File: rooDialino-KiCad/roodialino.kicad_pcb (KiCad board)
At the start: 2 copper layers, 65 x 30 mm, 54 parts, among them J1 Raspi Connector, J2 ICSP, J3 FTDI, J4 2nd IRX, J5 IR LED, Q1 2N7002, Q2 2N7002, Q3 2N7002, SW1 SW_Push, U1 ATmega328P, U2 TSOP34838, U3 TXS0108EPW, Y1 16 MHz

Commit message: Some final (?) bling
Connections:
- J5 pad 1: Net-(J5-Pad1) -> Net-(D8-Pad1)
- J5 pad 2: Net-(D8-Pad1) -> Net-(J5-Pad2)
- R11 pad 2: Net-(J5-Pad1) -> Net-(J5-Pad2)
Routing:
- net Net-(J5-Pad2): track 0.00 -> 6.35 mm
- net Net-(J5-Pad1): track 3.19 -> 0.00 mm
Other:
- board text removed: "A"

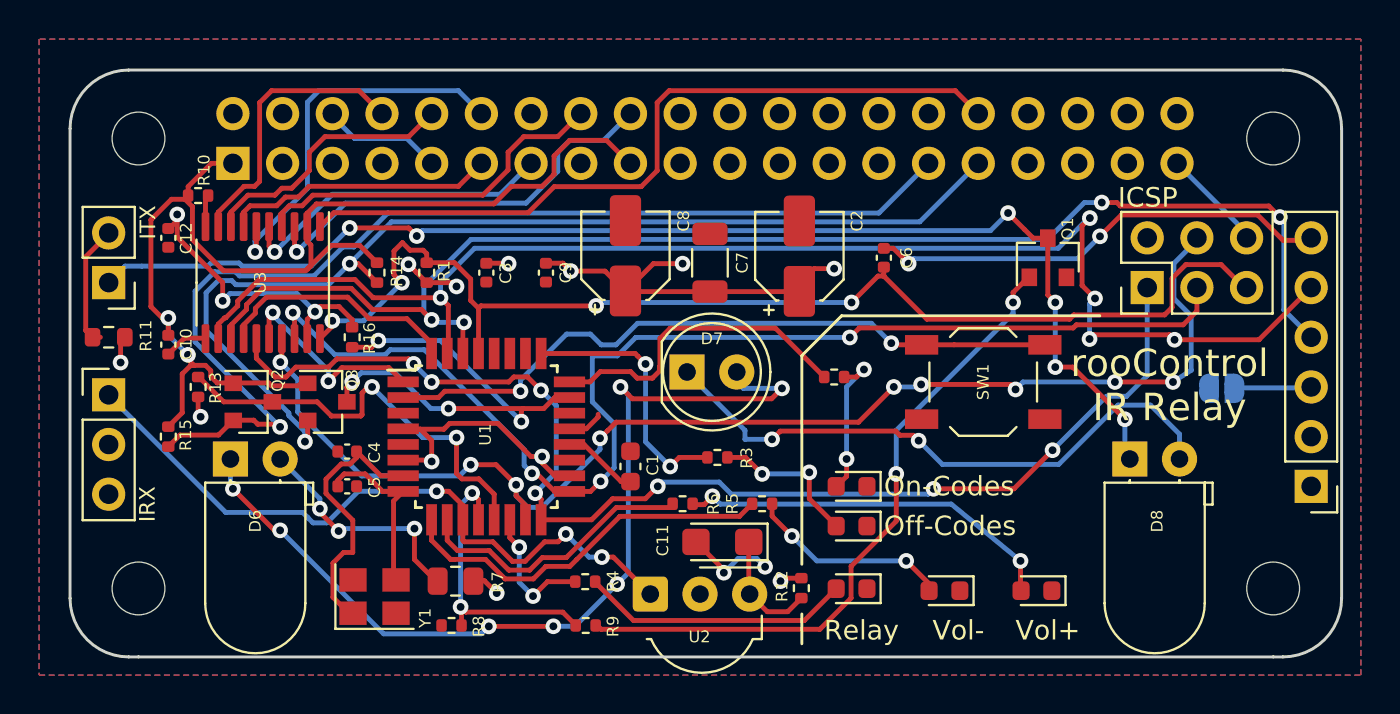
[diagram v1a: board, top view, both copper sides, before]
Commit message: Add Tooling Holes
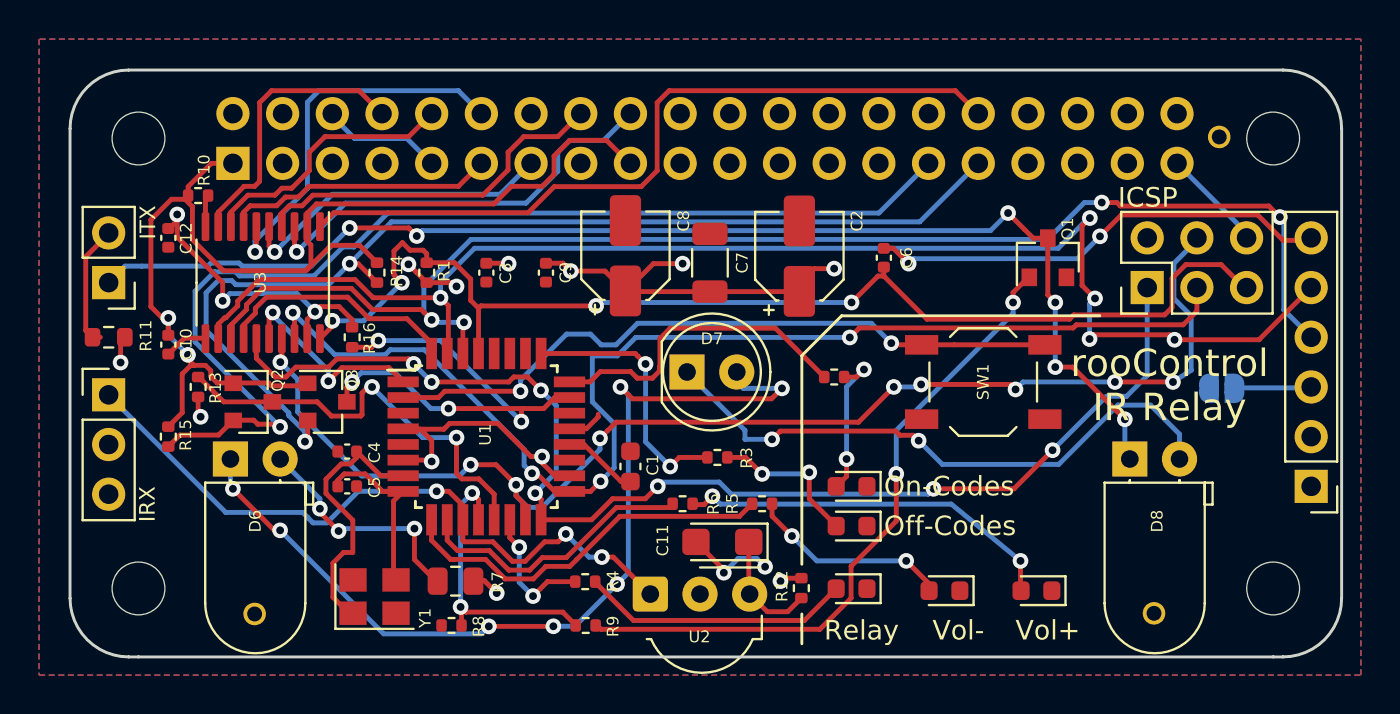
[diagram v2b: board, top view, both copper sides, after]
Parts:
- added REF**: JLCPCB Tooling Hole, MountingHole:JLCPCB Tooling Hole, F.Cu at (174.3, 92.5)
- added REF**: JLCPCB Tooling Hole, MountingHole:JLCPCB Tooling Hole, F.Cu at (170.9, 116.8)
- added REF**: JLCPCB Tooling Hole, MountingHole:JLCPCB Tooling Hole, F.Cu at (125.0, 116.9)
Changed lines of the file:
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@@
     (tracks 819)
     (zones 0)
-    (modules 54)
+    (modules 57)
     (nets 73)
   )
@@
     (add_net "Net-(U1-Pad28)")
   )
+  (module "MountingHole:JLCPCB Tooling Hole" (layer F.Cu)
+    (at 174.276 92.488)
+    (fp_text reference REF** (at 0.0254 2.0828) (layer F.SilkS) hide
+      (effects (font (size 1 1) (thickness 0.15)))
+    )
+    (fp_text value "JLCPCB Tooling Hole" (at -0.3556 -1.7272) (layer F.Fab)
+      (effects (font (size 1 1) (thickness 0.15)))
+    )
+    (pad "" np_thru_hole circle (at 2 2) (size 1.152 1.152) (drill 0.762) (layers *.Cu *.Mask)
+      (solder_mask_margin 0.148))
+  )
+  (module "MountingHole:JLCPCB Tooling Hole" (layer F.Cu)
+    (at 170.942 116.84)
+    (fp_text reference REF** (at 0.0254 2.0828) (layer F.SilkS) hide
+      (effects (font (size 1 1) (thickness 0.15)))
+    )
+    (fp_text value "JLCPCB Tooling Hole" (at -0.3556 -1.7272) (layer F.Fab)
+      (effects (font (size 1 1) (thickness 0.15)))
+    )
+    (pad "" np_thru_hole circle (at 2 2) (size 1.152 1.152) (drill 0.762) (layers *.Cu *.Mask)
+      (solder_mask_margin 0.148))
+  )
+  (module "MountingHole:JLCPCB Tooling Hole" (layer F.Cu)
+    (at 124.968 116.872)
+    (fp_text reference REF** (at 0.0254 2.0828) (layer F.SilkS) hide
+      (effects (font (size 1 1) (thickness 0.15)))
+    )
+    (fp_text value "JLCPCB Tooling Hole" (at -0.3556 -1.7272) (layer F.Fab)
+      (effects (font (size 1 1) (thickness 0.15)))
+    )
+    (pad "" np_thru_hole circle (at 2 2) (size 1.152 1.152) (drill 0.762) (layers *.Cu *.Mask)
+      (solder_mask_margin 0.148))
+  )
   (module Capacitor_Tantalum_SMD:CP_EIA-3216-18_Kemet-A (layer F.Cu)
     (at 150.876 115.189 180)
@@
       (effects (font (size 0.8 0.8) (thickness 0.12)))
     )
-    (pad 1 smd roundrect (at -1.35 0 180) (size 1.4 1.35) (layers F.Cu F.Paste F.Mask) (roundrect_rratio 0.185185)
+    (pad 1 smd roundrect (at -1.35 0 180) (size 1.4 1.35) (layers F.Cu F.Paste F.Mask) (roundrect_rratio 0.1851844444444445)
       (net 69 "Net-(C11-Pad1)"))
-    (pad 2 smd roundrect (at 1.35 0 180) (size 1.4 1.35) (layers F.Cu F.Paste F.Mask) (roundrect_rratio 0.185185)
+    (pad 2 smd roundrect (at 1.35 0 180) (size 1.4 1.35) (layers F.Cu F.Paste F.Mask) (roundrect_rratio 0.1851844444444445)
       (net 6 GNDD))
     (model ${KISYS3DMOD}/Capacitor_Tantalum_SMD.3dshapes/CP_EIA-3216-18_Kemet-A.wrl
@@
       (effects (font (size 0.5 0.5) (thickness 0.08)))
     )
-    (pad 1 smd roundrect (at -0.9125 0 180) (size 1.025 1.4) (layers F.Cu F.Paste F.Mask) (roundrect_rratio 0.2439014634146341)
+    (pad 1 smd roundrect (at -0.9125 0 180) (size 1.025 1.4) (layers F.Cu F.Paste F.Mask) (roundrect_rratio 0.2439004878048781)
       (net 2 +5V))
-    (pad 2 smd roundrect (at 0.9125 0 180) (size 1.025 1.4) (layers F.Cu F.Paste F.Mask) (roundrect_rratio 0.2439014634146341)
+    (pad 2 smd roundrect (at 0.9125 0 180) (size 1.025 1.4) (layers F.Cu F.Paste F.Mask) (roundrect_rratio 0.2439004878048781)
       (net 18 "Net-(D6-Pad2)"))
     (model ${KISYS3DMOD}/Resistor_SMD.3dshapes/R_0805_2012Metric.wrl
